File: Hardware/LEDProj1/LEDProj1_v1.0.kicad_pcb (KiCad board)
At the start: 2 copper layers, 21 x 20 mm, 6 parts, among them J1 Conn_01x02, SW1 SW_Push

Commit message: finished project 1!
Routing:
- net Net-(D1-K): track 0.00 -> 12.0 mm
- net Net-(D1-A): track 0.00 -> 5.92 mm
- net GND: track 0.00 -> 5.49 mm, vias 0 -> 1
- added copper zone on F.Cu, net +3V3
- added copper zone on B.Cu, net GND
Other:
- board size 21 x 20 mm -> 23 x 20.5 mm

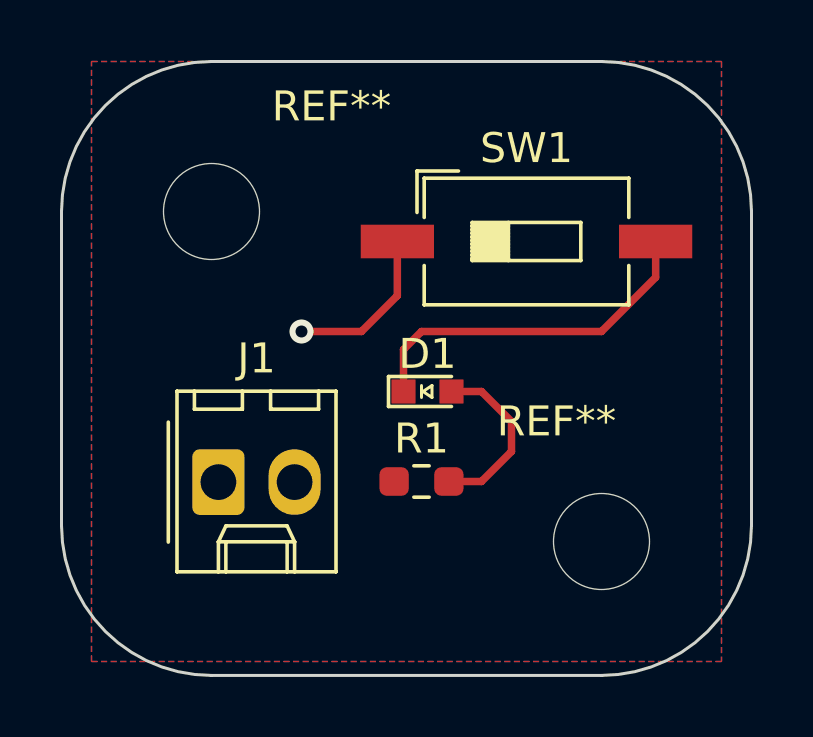
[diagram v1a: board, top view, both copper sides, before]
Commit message: Some edits were made to the PCB board components layout. - Eunsol
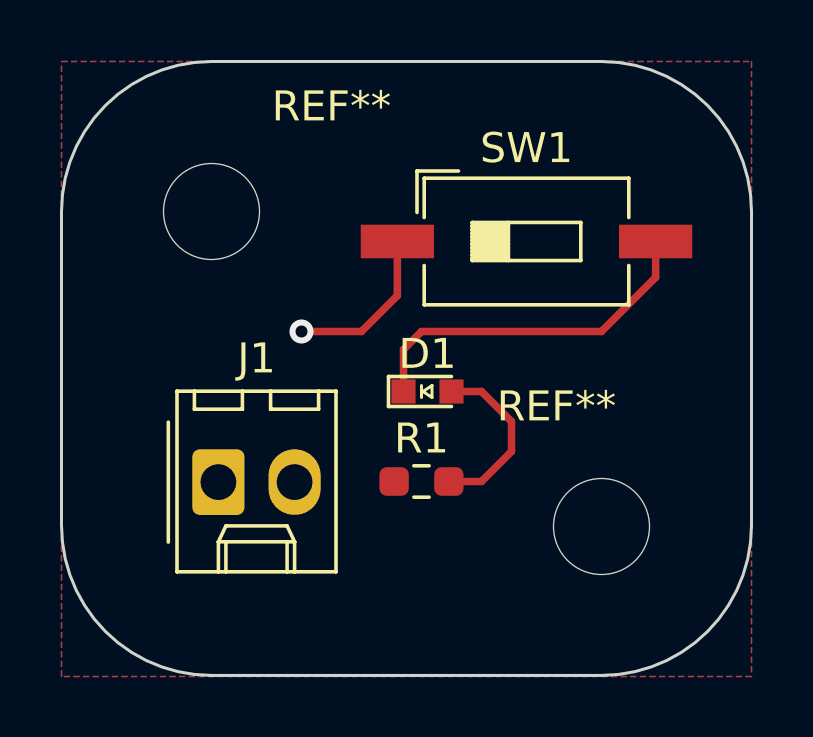
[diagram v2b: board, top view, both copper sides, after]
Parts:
- moved REF** 0.50 mm to (131.0, 91.5)
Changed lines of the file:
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@@
 	(footprint "MountingHole:MountingHole_3.2mm_M3"
 		(layer "F.Cu")
-		(at 131 92)
+		(at 131 91.5)
 		(descr "Mounting Hole 3.2mm, no annular, M3")
 		(tags "mounting hole 3.2mm no annular m3")
@@
 		(min_thickness 0.25)
 		(filled_areas_thickness no)
-		(fill yes
+		(fill
 			(thermal_gap 0.5)
 			(thermal_bridge_width 0.5)
@@
 		(polygon
 			(pts
-				(xy 114 76) (xy 135 76) (xy 135 96) (xy 114 96)
+				(xy 113 76) (xy 136 76) (xy 136 96.5) (xy 113 96.5)
 			)
 		)
@@
 		(min_thickness 0.25)
 		(filled_areas_thickness no)
-		(fill yes
+		(fill
 			(thermal_gap 0.5)
 			(thermal_bridge_width 0.5)
@@
 		(polygon
 			(pts
-				(xy 114 76) (xy 135 76) (xy 135 96) (xy 114 96)
-			)
-		)
+				(xy 113 76) (xy 136 76) (xy 136 96.5) (xy 113 96.5)
+			)
+		)
